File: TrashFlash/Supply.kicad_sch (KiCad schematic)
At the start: 0 parts

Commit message: Added Power Supply
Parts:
- added C15, C17: 10u, symbol Device:C
- added C16, C18: 22u, symbol Device:C
- added IC5, IC6: TPS63900DSKR, SON50P250X250X80-11N-D, symbol TrashFlash:TPS63900DSKR
- added L2, L3: 74438323100, INDC2520X100N, symbol TrashFlash:74438323100
- added R21, R24: 0, symbol Device:R
- added R22: 511, symbol Device:R
- added R23, R26: 36.5k, symbol Device:R
- added R25: 8.25k, symbol Device:R
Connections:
- new net: IC5.3 (CFG1), R23.1
- new net: IC5.4 (CFG2), R22.1
- new net: IC5.5 (CFG3), R21.1
- new net: IC5.7 (LX2), L2.2
- new net: IC5.9 (LX1), L2.1
- new net: IC6.3 (CFG1), R26.1
- new net: IC6.4 (CFG2), R25.1
- new net: IC6.5 (CFG3), R24.1
- new net: IC6.7 (LX2), L3.2
- new net: IC6.9 (LX1), L3.1
- new net 5V: C18.1, IC6.6 (VOUT)
- new net GND: C15.2, C16.2, C17.2, C18.2, IC5.11 (TP), IC5.8 (GND), IC6.11 (TP), IC6.8 (GND), R21.2, R22.2, R23.2, R24.2, R25.2, R26.2
- new net REG_5V_EN: IC6.1 (EN)
- new net SEL_VDD: IC5.2 (SEL)
- new net VDD: C16.1, IC5.6 (VOUT)
- new net VSYS: C15.1, C17.1, IC5.1 (EN), IC5.10 (VIN), IC6.10 (VIN), IC6.2 (SEL)
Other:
- note added: "1.8 V : RCFG1 = 0.00 kOhm, RCFG2 = 511 Ohm (100 mA Iin) 2.5 V : RCFG1 = 6.49 kOhm, RCFG2 = 511 Ohm (100 mA Iin) 3.3 V : RCFG1 = 36.5 kOhm, RCFG2 = 511 Ohm (100 mA Iin) 5.0 V : RCFG1 = 36.5 kOhm, RCFG2 = 8.25 kOhm (unlimited Iin)"
- note added: "HI: 3.3 V LO: 1.8 V"

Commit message: Added Battery Management
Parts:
- removed L2, L3: 74438323100, INDC2520X100N, symbol TrashFlash:74438323100
- added L4, L5: 74438343022, INDM2016X100N, symbol TrashFlash:74438343022
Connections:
- net at IC5.7 (LX2): now also L4.2
- net at IC5.9 (LX1): now also L4.1
- net at IC6.7 (LX2): now also L5.2
- net at IC6.9 (LX1): now also L5.1
- net REG_5V_EN renamed EN_REG_5V

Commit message: Added USB and powernets
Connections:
- net 5V renamed +5V

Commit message: Rotary encoder added + 3D stuff
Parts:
- C15, C16, C17, C18: footprint (none) -> Capacitor_SMD:C_0603_1608Metric
- IC5, IC6: footprint SON50P250X250X80-11N-D -> TrashFlash:SON50P250X250X80-11N-D
- L4, L5: footprint INDM2016X100N -> TrashFlash:INDM2016X100N
- R21, R22, R23, R24, R25, R26: footprint (none) -> Resistor_SMD:R_0402_1005Metric
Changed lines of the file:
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@@
 			)
 		)
-		(property "Footprint" "INDM2016X100N"
+		(property "Footprint" "TrashFlash:INDM2016X100N"
 			(at 162.56 193.98 0)
 			(effects
@@
 			)
 		)
-		(property "Footprint" "SON50P250X250X80-11N-D"
+		(property "Footprint" "TrashFlash:SON50P250X250X80-11N-D"
 			(at 162.56 131.75 0)
 			(effects
@@
 			)
 		)
-		(property "Footprint" ""
+		(property "Footprint" "Resistor_SMD:R_0402_1005Metric"
 			(at 172.212 64.77 90)
 			(effects
@@
 			)
 		)
-		(property "Footprint" "SON50P250X250X80-11N-D"
+		(property "Footprint" "TrashFlash:SON50P250X250X80-11N-D"
 			(at 162.56 201.6 0)
 			(effects
@@
 			)
 		)
-		(property "Footprint" ""
+		(property "Footprint" "Capacitor_SMD:C_0603_1608Metric"
 			(at 196.5452 53.34 0)
 			(effects
@@
 			)
 		)
-		(property "Footprint" ""
+		(property "Footprint" "Resistor_SMD:R_0402_1005Metric"
 			(at 182.372 64.77 90)
 			(effects
@@
 			)
 		)
-		(property "Footprint" ""
+		(property "Footprint" "Capacitor_SMD:C_0603_1608Metric"
 			(at 113.9952 53.34 0)
 			(effects
@@
 			)
 		)
-		(property "Footprint" ""
+		(property "Footprint" "Resistor_SMD:R_0402_1005Metric"
 			(at 172.212 134.62 90)
 			(effects
@@
 			)
 		)
-		(property "Footprint" "INDM2016X100N"
+		(property "Footprint" "TrashFlash:INDM2016X100N"
 			(at 162.56 124.13 0)
 			(effects
@@
 			)
 		)
-		(property "Footprint" ""
+		(property "Footprint" "Capacitor_SMD:C_0603_1608Metric"
 			(at 196.5452 124.46 0)
 			(effects
@@
 			)
 		)
-		(property "Footprint" ""
+		(property "Footprint" "Resistor_SMD:R_0402_1005Metric"
 			(at 162.052 64.77 90)
 			(effects
@@
 			)
 		)
-		(property "Footprint" ""
+		(property "Footprint" "Resistor_SMD:R_0402_1005Metric"
 			(at 182.372 134.62 90)
 			(effects
@@
 			)
 		)
-		(property "Footprint" ""
+		(property "Footprint" "Capacitor_SMD:C_0603_1608Metric"
 			(at 113.9952 123.19 0)
 			(effects
@@
 			)
 		)
-		(property "Footprint" ""
+		(property "Footprint" "Resistor_SMD:R_0402_1005Metric"
 			(at 162.052 134.62 90)
 			(effects

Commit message: Footprints 3D model fixed
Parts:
- IC5, IC6: footprint TrashFlash:SON50P250X250X80-11N-D -> SON50P250X250X80-11N-D
- L4, L5: footprint TrashFlash:INDM2016X100N -> INDM2016X100N
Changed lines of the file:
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@@
 			)
 		)
-		(property "Footprint" "TrashFlash:INDM2016X100N"
+		(property "Footprint" "INDM2016X100N"
 			(at 162.56 193.98 0)
 			(effects
@@
 			)
 		)
-		(property "Footprint" "TrashFlash:SON50P250X250X80-11N-D"
+		(property "Footprint" "SON50P250X250X80-11N-D"
 			(at 162.56 131.75 0)
 			(effects
@@
 			)
 		)
-		(property "Footprint" "TrashFlash:SON50P250X250X80-11N-D"
+		(property "Footprint" "SON50P250X250X80-11N-D"
 			(at 162.56 201.6 0)
 			(effects
@@
 			)
 		)
-		(property "Footprint" "TrashFlash:INDM2016X100N"
+		(property "Footprint" "INDM2016X100N"
 			(at 162.56 124.13 0)
 			(effects

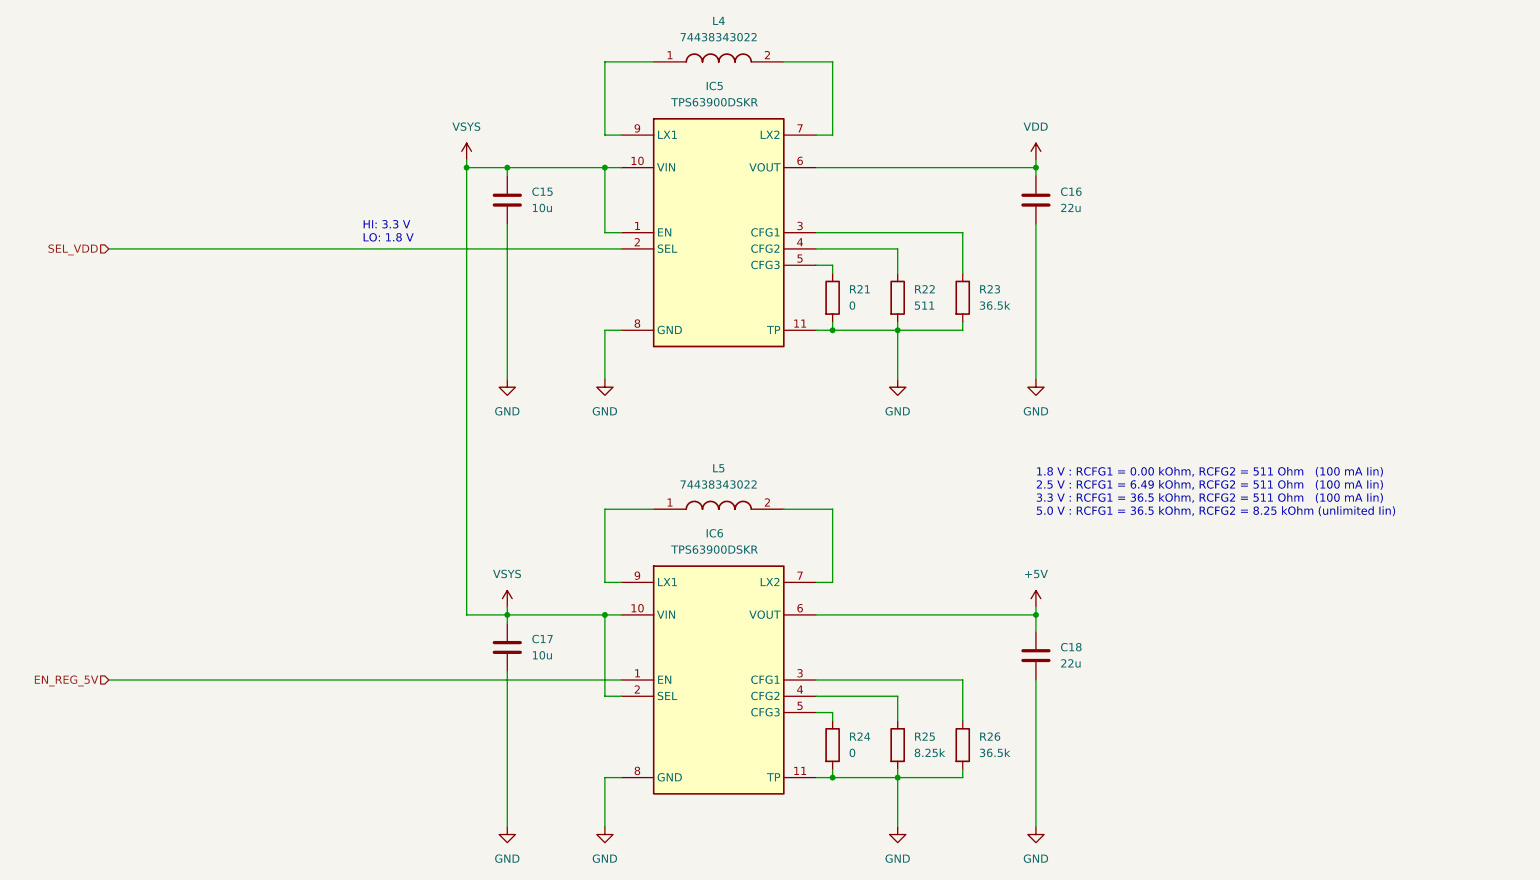
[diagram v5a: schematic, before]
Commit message: Added netlabels / cleaned up schematic
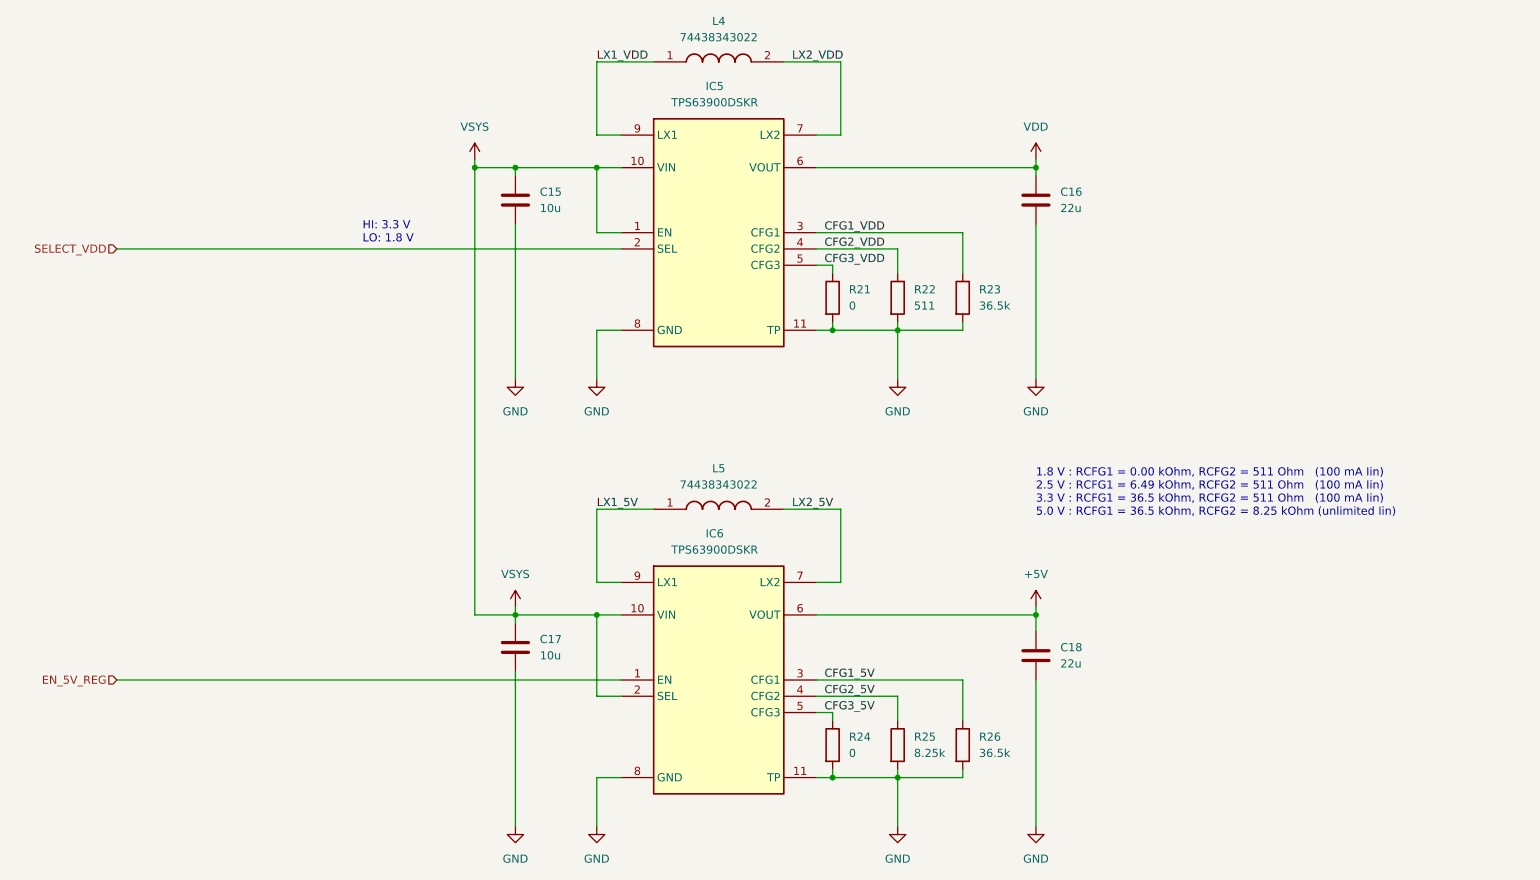
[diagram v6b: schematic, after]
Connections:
- net LX1_5V: now reaches IC6.9 (LX1), L5.1
- net LX2_5V: now reaches IC6.7 (LX2), L5.2
- net CFG1_VDD: now reaches IC5.3 (CFG1), R23.1
- net CFG2_VDD: now reaches IC5.4 (CFG2), R22.1
- net CFG3_VDD: now reaches IC5.5 (CFG3), R21.1
- net LX2_VDD: now reaches IC5.7 (LX2), L4.2
- net LX1_VDD: now reaches IC5.9 (LX1), L4.1
- net CFG1_5V: now reaches IC6.3 (CFG1), R26.1
- net CFG2_5V: now reaches IC6.4 (CFG2), R25.1
- net CFG3_5V: now reaches IC6.5 (CFG3), R24.1
- net EN_REG_5V renamed EN_5V_REG
- net SEL_VDD renamed SELECT_VDD
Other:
- moved on the sheet: C15, C17

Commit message: Added 3D-models to footprints, PCB outline and component placement
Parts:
- IC5, IC6: footprint SON50P250X250X80-11N-D -> TrashFlash:SON50P250X250X80-11N-D
- L4, L5: footprint INDM2016X100N -> TrashFlash:INDM2016X100N
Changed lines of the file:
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@@
 			)
 		)
-		(property "Footprint" "INDM2016X100N"
+		(property "Footprint" "TrashFlash:INDM2016X100N"
 			(at 162.56 193.98 0)
 			(effects
@@
 			)
 		)
-		(property "Footprint" "SON50P250X250X80-11N-D"
+		(property "Footprint" "TrashFlash:SON50P250X250X80-11N-D"
 			(at 162.56 131.75 0)
 			(effects
@@
 			)
 		)
-		(property "Footprint" "SON50P250X250X80-11N-D"
+		(property "Footprint" "TrashFlash:SON50P250X250X80-11N-D"
 			(at 162.56 201.6 0)
 			(effects
@@
 			)
 		)
-		(property "Footprint" "INDM2016X100N"
+		(property "Footprint" "TrashFlash:INDM2016X100N"
 			(at 162.56 124.13 0)
 			(effects

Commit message: Added Wireless and inter PCB connector
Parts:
- removed R21: 0, Resistor_SMD:R_0402_1005Metric, symbol Device:R
- IC501: renamed from IC5; footprint TrashFlash:SON50P250X250X80-11N-D -> SON50P250X250X80-11N-D
- IC502: renamed from IC6; footprint TrashFlash:SON50P250X250X80-11N-D -> SON50P250X250X80-11N-D
- L501: renamed from L4; footprint TrashFlash:INDM2016X100N -> INDM2016X100N
- L502: renamed from L5; footprint TrashFlash:INDM2016X100N -> INDM2016X100N
- R502: renamed from R23; value 36.5k -> 6.49k
- renumbered C15 to C501, C16 to C502, C17 to C503, C18 to C504, R22 to R501, R24 to R503, R25 to R504, R26 to R505
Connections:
- net CFG3_VDD is gone; now on net GND: IC501.5 (CFG3)
- net SELECT_VDD is gone; now on net VSYS: IC501.2 (SEL)
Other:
- note added: "2.5 V : RCFG1 = 6.49 kOhm, RCFG2 = 511 Ohm (100 mA Iin) 5.0 V : RCFG1 = 36.5 kOhm, RCFG2 = 8.25 kOhm (unlimited Iin)"
- note removed: "1.8 V : RCFG1 = 0.00 kOhm, RCFG2 = 511 Ohm (100 mA Iin) 2.5 V : RCFG1 = 6.49 kOhm, RCFG2 = 511 Ohm (100 mA Iin) 3.3 V : RCFG1 = 36.5 kOhm, RCFG2 = 511 Ohm (100 mA Iin) 5.0 V : RCFG1 = 36.5 kOhm, RCFG2 = 8.25 kOhm (unlimited Iin)"
- note removed: "HI: 3.3 V LO: 1.8 V"
